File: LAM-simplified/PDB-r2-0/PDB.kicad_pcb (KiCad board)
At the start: 2 copper layers, 115 x 115 mm, 23 parts, among them J1 2.54mm 2x3, J10 xt60-female, J11 xt60-female, J12 xt60-female, J13 xt90-female, J14 xt90-female, J15 2.54mm 2x3, J2 2.54mm 2x3, J3 2.54mm 2x3, J5 xt30-female, J6 xt30-female, J7 xt60-female, J8 xt60-female, J9 xt60-female

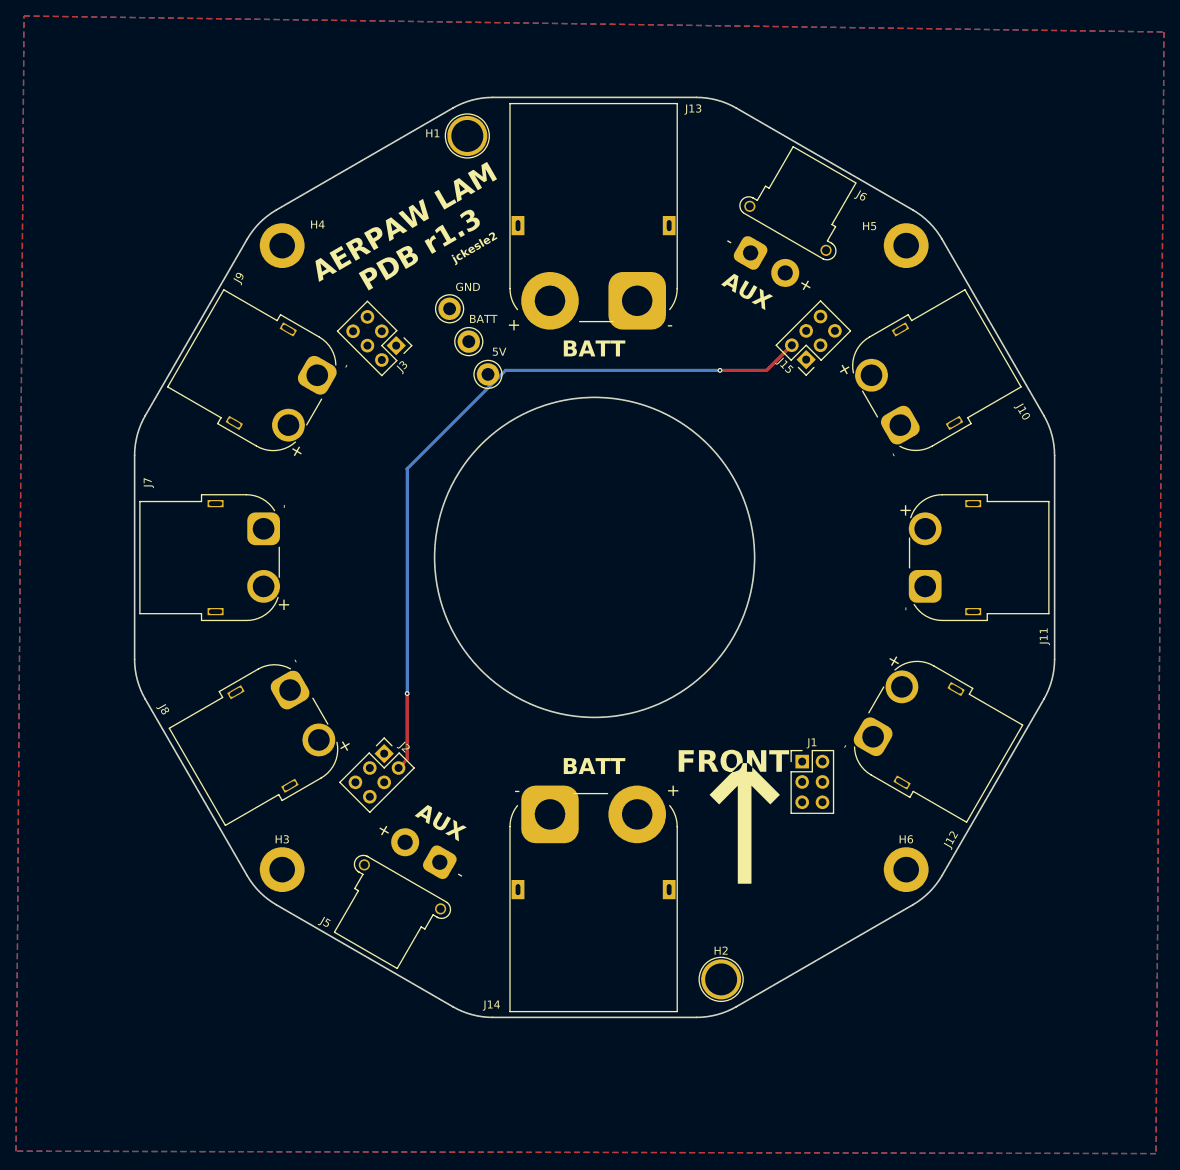
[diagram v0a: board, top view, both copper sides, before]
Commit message: add AS150s to PDB r2.0
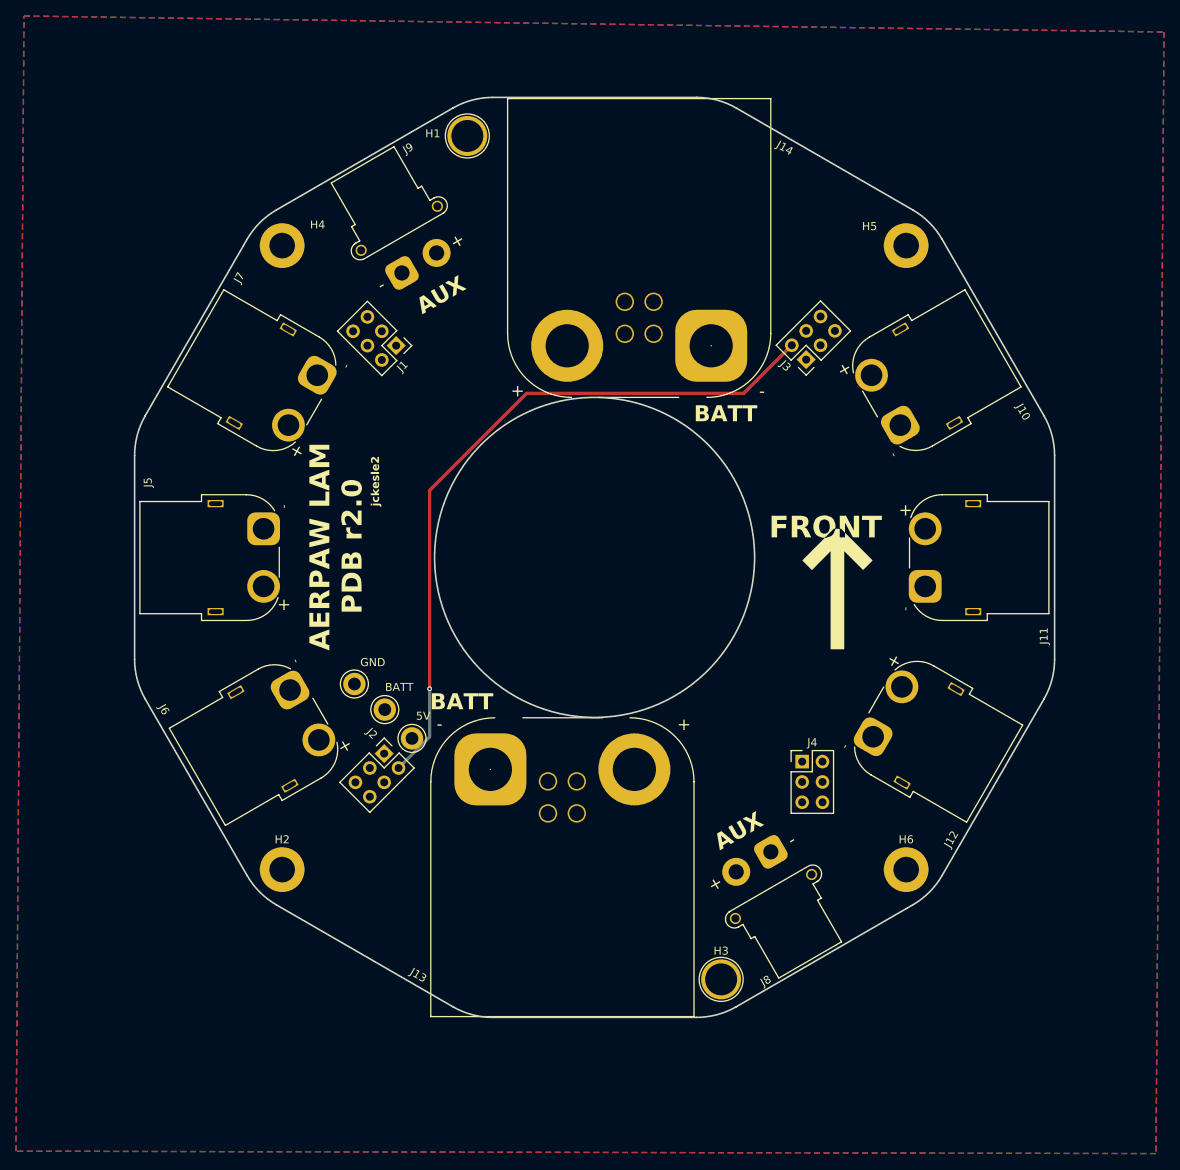
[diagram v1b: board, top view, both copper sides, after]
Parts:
- J13, J14: value xt90-female -> AS150UPW-M(ale); footprint aerpaw-footprints:AMASS_XT90PW-F -> aerpaw-footprints:AS150UPW(2+4-)M.G.Y
- moved J13 93.5 mm to (159.8, 159.0), turned to 180 degrees
- moved J14 93.5 mm to (169.4, 36.2), turned to 0 degrees
- moved GND 48.4 mm to (133.8, 113.4)
- moved BATT 47.2 mm to (137.6, 116.6)
- moved 5V 46.5 mm to (141.0, 120.2)
- moved J9 43.7 mm to (139.7, 62.0), turned to 30 degrees
- moved J8 41.4 mm to (185.9, 134.4), turned to -150 degrees
- renumbered H3 to H2, H2 to H3, J3 to J1, J15 to J3, J1 to J4, J7 to J5, J8 to J6, J9 to J7, J5 to J8, J6 to J9
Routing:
- net +5V: track 92.3 -> 89.1 mm, vias 2 -> 1
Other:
- board text added: "AERPAW LAM PDB r2.0"
- board text removed: "AERPAW LAM PDB r1.3"

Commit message: add jlc manufacturing files
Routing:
- net +5V: track 89.1 -> 4.40 mm, vias 1 -> 0
